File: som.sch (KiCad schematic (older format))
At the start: 22 parts, among them M1 SC606T

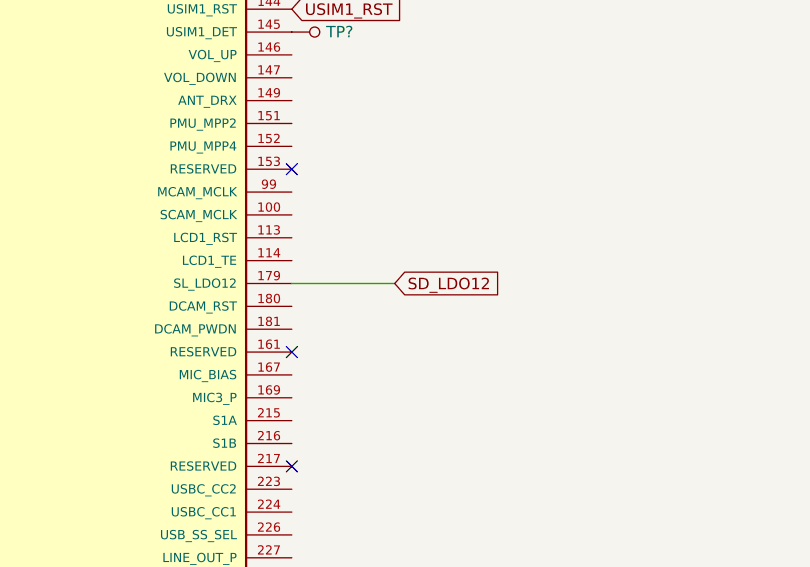
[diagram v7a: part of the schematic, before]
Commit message: Added ESD protection to SD card
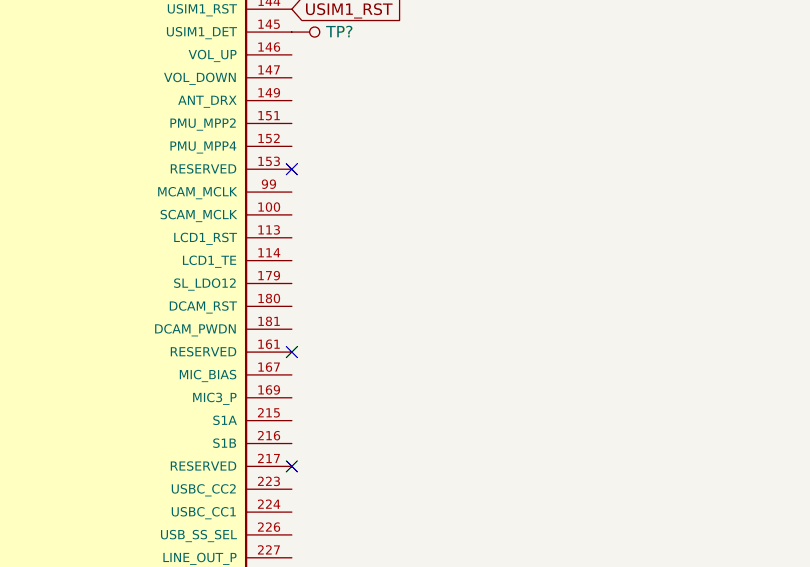
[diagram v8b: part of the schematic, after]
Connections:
- net SD_LDO12: no longer names the net of M1.179 (SL_LDO12)
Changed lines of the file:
@@
 Wire Wire Line
 	1600 4500 2000 4500
-Text GLabel 5450 4250 2    50   Input ~ 0
-SD_LDO12
-Wire Wire Line
-	5450 4250 5000 4250
 Text GLabel 2450 1650 0    50   Input ~ 0
 LDO5_1P8
 Wire Wire Line
 	2450 1650 2800 1650
+Text GLabel 5000 2350 2    50   Input ~ 0
+ANT_GNSS
+Text GLabel 2800 2550 0    50   Input ~ 0
+ANT_MAIN
 Wire Bus Line
 	1750 4650 1750 5350
@@
 Wire Bus Line
 	11650 7800 11650 8700
-Text GLabel 5000 2350 2    50   Input ~ 0
-ANT_GNSS
-Text GLabel 2800 2550 0    50   Input ~ 0
-ANT_MAIN
 $EndSCHEMATC
